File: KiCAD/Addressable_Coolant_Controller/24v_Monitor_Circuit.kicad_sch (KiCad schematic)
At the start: 4 parts, among them U10 PC12311NSZ1B

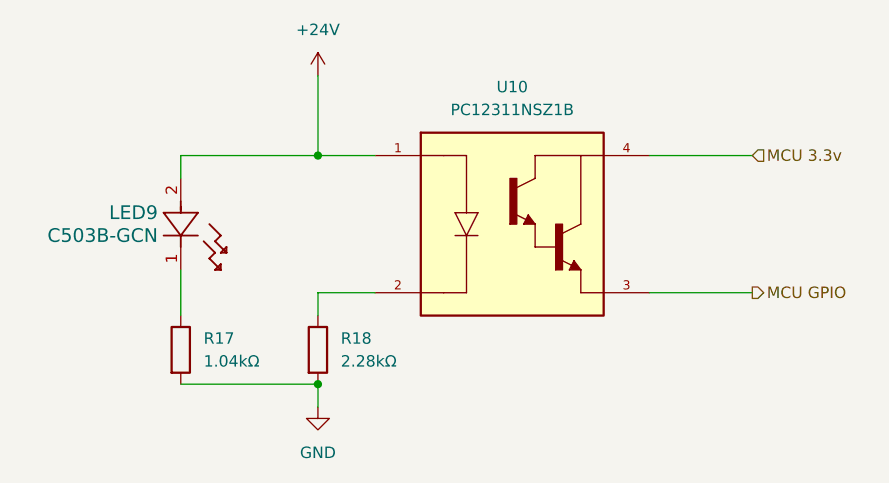
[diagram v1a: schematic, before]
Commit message: Added voltage divider and changed to 12 pin connectors
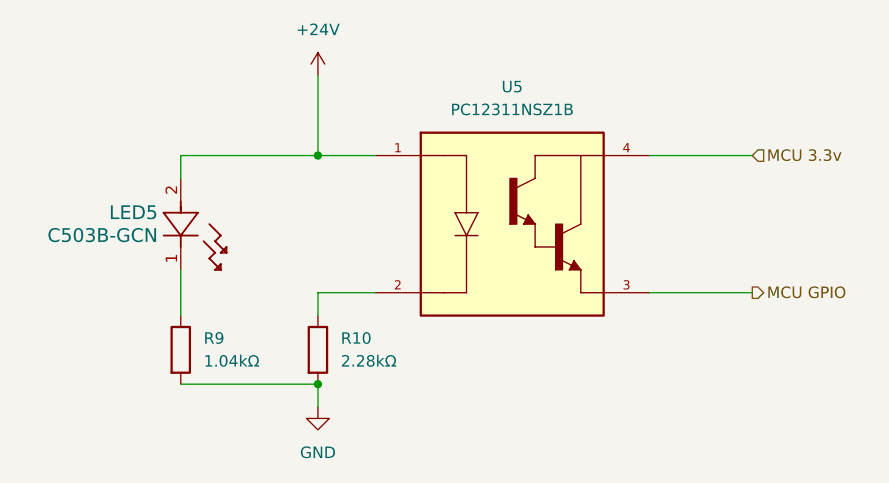
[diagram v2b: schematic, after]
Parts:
- renumbered LED9 to LED5, R18 to R10, R17 to R9, U10 to U5
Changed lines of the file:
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@@
   (symbol (lib_id "PC12311NSZ1B:PC12311NSZ1B") (at 134.62 93.98 0) (unit 1)
     (in_bom yes) (on_board yes) (dnp no) (fields_autoplaced)
-    (property "Reference" "U10" (at 133.35 77.47 0)
+    (property "Reference" "U5" (at 133.35 77.47 0)
       (effects (font (size 1.27 1.27)))
     )
@@
       (project "Addressable_Coolant_Controller"
         (path "/603d0a2e-fca7-40af-8fa8-51b59d823d4d/9e308de8-a8a3-4754-85bb-a6ac18661119/5975585f-6378-4874-929c-f4a5e89e51e7"
-          (reference "U10") (unit 1)
+          (reference "U5") (unit 1)
         )
       )
@@
   (symbol (lib_id "Device:R") (at 96.52 106.68 0) (unit 1)
     (in_bom yes) (on_board yes) (dnp no) (fields_autoplaced)
-    (property "Reference" "R17" (at 99.06 105.41 0)
+    (property "Reference" "R9" (at 99.06 105.41 0)
       (effects (font (size 1.27 1.27)) (justify left))
     )
@@
       (project "Addressable_Coolant_Controller"
         (path "/603d0a2e-fca7-40af-8fa8-51b59d823d4d/9e308de8-a8a3-4754-85bb-a6ac18661119/5975585f-6378-4874-929c-f4a5e89e51e7"
-          (reference "R17") (unit 1)
+          (reference "R9") (unit 1)
         )
       )
@@
   (symbol (lib_id "CreeLED Green:C503B-GCN-CY0C0792") (at 96.52 87.63 270) (unit 1)
     (in_bom yes) (on_board yes) (dnp no)
-    (property "Reference" "LED9" (at 93.98 91.44 90)
+    (property "Reference" "LED5" (at 93.98 91.44 90)
       (effects (font (size 1.524 1.524)) (justify right))
     )
@@
       (project "Addressable_Coolant_Controller"
         (path "/603d0a2e-fca7-40af-8fa8-51b59d823d4d/9e308de8-a8a3-4754-85bb-a6ac18661119/5975585f-6378-4874-929c-f4a5e89e51e7"
-          (reference "LED9") (unit 1)
+          (reference "LED5") (unit 1)
         )
       )
@@
   (symbol (lib_id "Device:R") (at 111.76 106.68 0) (unit 1)
     (in_bom yes) (on_board yes) (dnp no) (fields_autoplaced)
-    (property "Reference" "R18" (at 114.3 105.41 0)
+    (property "Reference" "R10" (at 114.3 105.41 0)
       (effects (font (size 1.27 1.27)) (justify left))
     )
@@
       (project "Addressable_Coolant_Controller"
         (path "/603d0a2e-fca7-40af-8fa8-51b59d823d4d/9e308de8-a8a3-4754-85bb-a6ac18661119/5975585f-6378-4874-929c-f4a5e89e51e7"
-          (reference "R18") (unit 1)
+          (reference "R10") (unit 1)
         )
       )

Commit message: Fixed broken netclasses, removed voltage divider circuit
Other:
- company: (none) -> Warner Consulting Inc.
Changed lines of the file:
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@@
 (kicad_sch (version 20230121) (generator eeschema)
   (paper "A4")
+  (title_block
+    (company "Warner Consulting Inc.")
+  )
   (junction (at 111.76 110.49) (diameter 0) (color 0 0 0 0)
   )

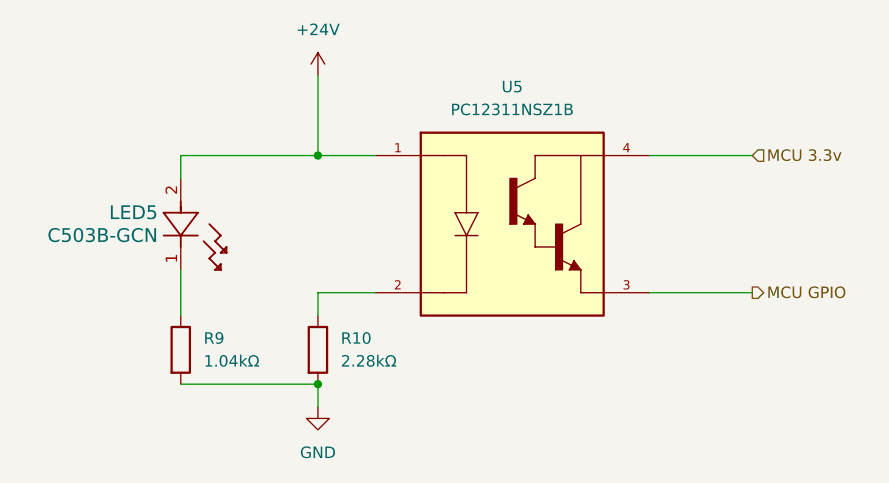
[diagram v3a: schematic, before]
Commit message: Added second board outline and circular connectors
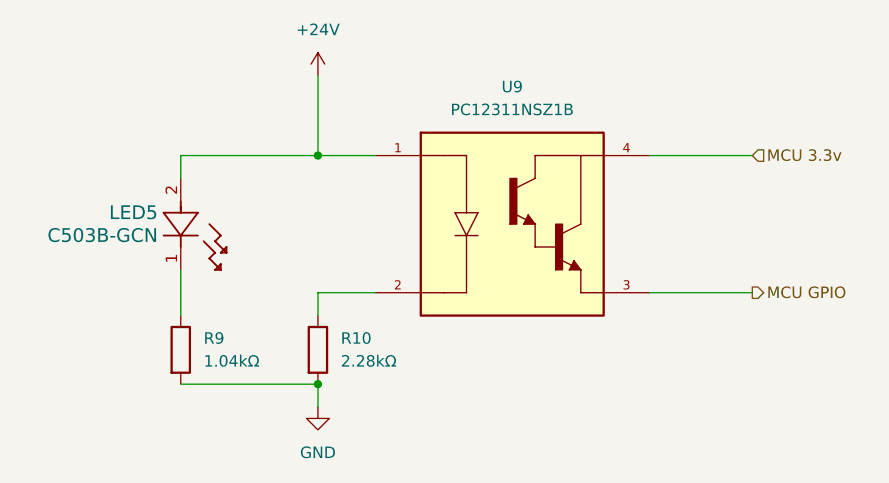
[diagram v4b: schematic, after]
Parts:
- renumbered U5 to U9
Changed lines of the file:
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@@
   (symbol (lib_id "power:+24V") (at 111.76 76.2 0) (unit 1)
     (in_bom yes) (on_board yes) (dnp no) (fields_autoplaced)
-    (property "Reference" "#PWR019" (at 111.76 80.01 0)
+    (property "Reference" "#PWR0101" (at 111.76 80.01 0)
       (effects (font (size 1.27 1.27)) hide)
     )
@@
       (project "Addressable_Coolant_Controller"
         (path "/603d0a2e-fca7-40af-8fa8-51b59d823d4d/9e308de8-a8a3-4754-85bb-a6ac18661119/5975585f-6378-4874-929c-f4a5e89e51e7"
-          (reference "#PWR019") (unit 1)
+          (reference "#PWR0101") (unit 1)
         )
       )
@@
   (symbol (lib_id "PC12311NSZ1B:PC12311NSZ1B") (at 134.62 93.98 0) (unit 1)
     (in_bom yes) (on_board yes) (dnp no) (fields_autoplaced)
-    (property "Reference" "U5" (at 133.35 77.47 0)
+    (property "Reference" "U9" (at 133.35 77.47 0)
       (effects (font (size 1.27 1.27)))
     )
@@
       (project "Addressable_Coolant_Controller"
         (path "/603d0a2e-fca7-40af-8fa8-51b59d823d4d/9e308de8-a8a3-4754-85bb-a6ac18661119/5975585f-6378-4874-929c-f4a5e89e51e7"
-          (reference "U5") (unit 1)
+          (reference "U9") (unit 1)
         )
       )
@@
   (symbol (lib_id "power:GND") (at 111.76 113.03 0) (unit 1)
     (in_bom yes) (on_board yes) (dnp no) (fields_autoplaced)
-    (property "Reference" "#PWR020" (at 111.76 119.38 0)
+    (property "Reference" "#PWR0102" (at 111.76 119.38 0)
       (effects (font (size 1.27 1.27)) hide)
     )
@@
       (project "Addressable_Coolant_Controller"
         (path "/603d0a2e-fca7-40af-8fa8-51b59d823d4d/9e308de8-a8a3-4754-85bb-a6ac18661119/5975585f-6378-4874-929c-f4a5e89e51e7"
-          (reference "#PWR020") (unit 1)
+          (reference "#PWR0102") (unit 1)
         )
       )

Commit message: Routed connector PCB and fixed components designators
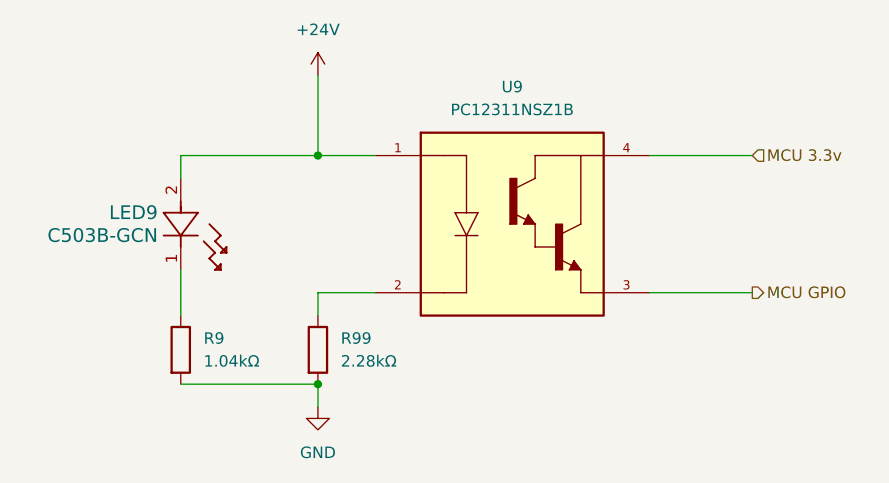
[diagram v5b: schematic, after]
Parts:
- renumbered LED5 to LED9, R10 to R99
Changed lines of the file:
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@@
   (symbol (lib_id "CreeLED Green:C503B-GCN-CY0C0792") (at 96.52 87.63 270) (unit 1)
     (in_bom yes) (on_board yes) (dnp no)
-    (property "Reference" "LED5" (at 93.98 91.44 90)
+    (property "Reference" "LED9" (at 93.98 91.44 90)
       (effects (font (size 1.524 1.524)) (justify right))
     )
@@
       (project "Addressable_Coolant_Controller"
         (path "/603d0a2e-fca7-40af-8fa8-51b59d823d4d/9e308de8-a8a3-4754-85bb-a6ac18661119/5975585f-6378-4874-929c-f4a5e89e51e7"
-          (reference "LED5") (unit 1)
+          (reference "LED9") (unit 1)
         )
       )
@@
   (symbol (lib_id "Device:R") (at 111.76 106.68 0) (unit 1)
     (in_bom yes) (on_board yes) (dnp no) (fields_autoplaced)
-    (property "Reference" "R10" (at 114.3 105.41 0)
+    (property "Reference" "R99" (at 114.3 105.41 0)
       (effects (font (size 1.27 1.27)) (justify left))
     )
@@
       (project "Addressable_Coolant_Controller"
         (path "/603d0a2e-fca7-40af-8fa8-51b59d823d4d/9e308de8-a8a3-4754-85bb-a6ac18661119/5975585f-6378-4874-929c-f4a5e89e51e7"
-          (reference "R10") (unit 1)
+          (reference "R99") (unit 1)
         )
       )

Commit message: Updating Cree LED footprints with STEP files
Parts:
- LED9: footprint CreeLED Green:C503B_GCN_CY0C0792 -> C503B_GCN_CY0C0792:C503B_GCN_CY0C0792
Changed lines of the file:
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@@
       (effects (font (size 1.524 1.524)) (justify right))
     )
-    (property "Footprint" "CreeLED Green:C503B_GCN_CY0C0792" (at 96.52 87.63 0)
+    (property "Footprint" "C503B_GCN_CY0C0792:C503B_GCN_CY0C0792" (at 96.52 87.63 0)
       (effects (font (size 1.27 1.27) italic) hide)
     )
